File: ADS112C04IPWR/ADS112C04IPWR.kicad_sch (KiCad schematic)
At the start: 3 parts, among them J1 Conn_01x08, J2 Conn_01x08, U1 ADS112C04IPWR

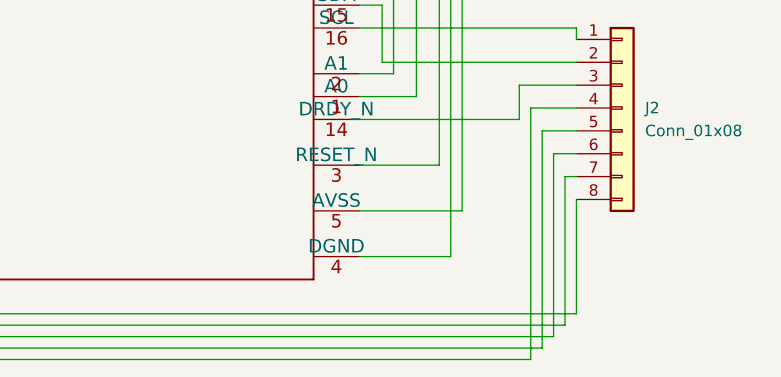
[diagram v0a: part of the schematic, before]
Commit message: Updating the ADC
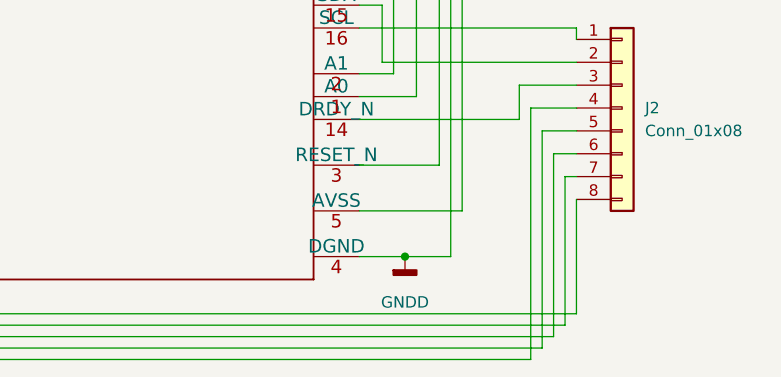
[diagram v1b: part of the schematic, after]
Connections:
- net GNDD: now reaches J1.4 (Pin_4), U1.4 (DGND)
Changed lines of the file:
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@@
     (date "2022-02-26")
   )
+  (junction (at 167.64 109.22) (diameter 0) (color 0 0 0 0)
+  )
   (wire (pts (xy 168.91 64.77) (xy 82.55 64.77))
     (stroke (width 0) (type default) (color 0 0 0 0))
@@
     (stroke (width 0) (type default) (color 0 0 0 0))
   )
+  (wire (pts (xy 167.64 109.22) (xy 172.72 109.22))
+    (stroke (width 0) (type default) (color 0 0 0 0))
+  )
   (wire (pts (xy 184.15 118.11) (xy 184.15 97.79))
     (stroke (width 0) (type default) (color 0 0 0 0))
   )
-  (wire (pts (xy 162.56 109.22) (xy 172.72 109.22))
+  (wire (pts (xy 162.56 109.22) (xy 167.64 109.22))
     (stroke (width 0) (type default) (color 0 0 0 0))
   )
@@
   (wire (pts (xy 162.56 93.98) (xy 180.34 93.98))
     (stroke (width 0) (type default) (color 0 0 0 0))
+  )
+  (symbol (lib_id "power:GNDD") (at 167.64 109.22 0) (unit 1)
+    (in_bom yes) (on_board yes) (fields_autoplaced)
+    (property "Reference" "#PWR0101" (id 0) (at 167.64 115.57 0)
+      (effects (font (size 1.27 1.27)) hide)
+    )
+    (property "Value" "GNDD" (id 1) (at 167.64 114.3 0))
+    (property "Footprint" "" (id 2) (at 167.64 109.22 0)
+      (effects (font (size 1.27 1.27)) hide)
+    )
+    (property "Datasheet" "" (id 3) (at 167.64 109.22 0)
+      (effects (font (size 1.27 1.27)) hide)
+    )
+    (pin "1")
   )
   (symbol (lib_id "Connector_Generic:Conn_01x08") (at 77.47 91.44 0) (mirror y) (unit 1)
@@
   )
   (symbol_instances
+    (path "/3c44e781-1190-4e9e-8bbc-c825cbc80c09"
+      (reference "#PWR0101") (unit 1) (value "GNDD") (footprint "")
+    )
     (path "/4edb63b2-0c13-41c4-bb44-548af3740a27"
       (reference "J1") (unit 1) (value "Conn_01x08") (footprint "Connector_PinHeader_2.54mm:PinHeader_1x08_P2.54mm_Vertical")

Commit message: Revision One
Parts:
- removed J1, J2: Conn_01x08, Connector_PinHeader_2.54mm:PinHeader_1x08_P2.54mm_Vertical, symbol Connector_Generic:Conn_01x08
- added C1, C2: 0.1μF, Capacitor_SMD:C_0201_0603Metric_Pad0.64x0.40mm_HandSolder, symbol Device:C
- added J1, J2: Conn_01x04, Connector_PinHeader_2.54mm:PinHeader_1x04_P2.54mm_Vertical, symbol Connector_Generic:Conn_01x04
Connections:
- net GNDD is gone; now on net GND: U1.4 (DGND)
- net SCL: now reaches U1.1 (A0)
- net SCL: now also U1.16 (SCL), U1.2 (A1), J1.4 (Pin_4)
- net +3V3: now reaches U1.3 (RESET_N)
- net +3V3: now also U1.12 (AVDD), U1.13 (DVDD), C1.1, C2.1, J2.3 (Pin_3)
- net GND: now reaches U1.5 (AVSS)
- net GND: now also C1.2, C2.2, J2.4 (Pin_4)
- net AIN3: now reaches U1.6 (AIN3)
- net AIN3: now also J2.2 (Pin_2)
- net AIN2: now reaches U1.7 (AIN2)
- net AIN2: now also J2.1 (Pin_1)
- net AIN1: now reaches U1.10 (AIN1)
- net AIN1: now also J1.1 (Pin_1)
- net AIN0: now reaches U1.11 (AIN0)
- net AIN0: now also J1.2 (Pin_2)
- net SDA: now reaches U1.15 (SDA)
- net SDA: now also J1.3 (Pin_3)
- no-connect marks 0 -> 3
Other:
- note added: "Tying A1 and A0 to SCL creates I²C address 100 1111 (0x4F) SDA and SCL REQUIRE pullup resistors"
